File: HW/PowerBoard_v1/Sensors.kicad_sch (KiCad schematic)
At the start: 46 parts, among them U3 MCP9700AT-ETT, U4 PAMC1350DWVR, U5 PAMC1350DWVR, U6 PAMC1350DWVR, U7 PAMC1350DWVR, U8 3v3 ISO DC/DC

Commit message: updated naming
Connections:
- net SHUNT OUT is gone; now on net Batt In: R11.1, TP11.1, U7.2 (INP)
- net Batt IN+ renamed Batt In
- net Batt Out+ renamed Batt Out
- net SHUNT IN renamed Sol Out
- net Solar IN+ renamed Sol In
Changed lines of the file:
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@@
 		)
 	)
+	(wire
+		(pts
+			(xy 245.11 129.54) (xy 255.27 129.54)
+		)
+		(stroke
+			(width 0)
+			(type default)
+		)
+	)
 	(polyline
 		(pts
@@
 	(wire
 		(pts
-			(xy 259.08 134.62) (xy 245.11 134.62)
+			(xy 255.27 134.62) (xy 245.11 134.62)
 		)
 		(stroke
@@
 	(wire
 		(pts
-			(xy 245.11 139.7) (xy 259.08 139.7)
+			(xy 245.11 139.7) (xy 255.27 139.7)
 		)
 		(stroke
@@
 	(wire
 		(pts
-			(xy 259.08 129.54) (xy 245.11 129.54)
-		)
-		(stroke
-			(width 0)
-			(type default)
-		)
-	)
-	(wire
-		(pts
 			(xy 127 71.12) (xy 124.46 71.12)
 		)
@@
 	(wire
 		(pts
-			(xy 245.11 124.46) (xy 259.08 124.46)
+			(xy 245.11 124.46) (xy 255.27 124.46)
 		)
 		(stroke
@@
 		)
 	)
-	(label "I- Sense Batt"
-		(at 179.07 146.05 180)
+	(label "Sol Out"
+		(at 265.43 83.82 180)
 		(fields_autoplaced yes)
 		(effects
@@
 		)
 	)
-	(label "ADC V Batt"
-		(at 53.34 38.1 180)
+	(label "Batt In"
+		(at 179.07 143.51 180)
 		(fields_autoplaced yes)
 		(effects
@@
 		)
 	)
-	(label "I- Sense Sol"
-		(at 265.43 83.82 180)
+	(label "ADC V Batt"
+		(at 53.34 38.1 180)
 		(fields_autoplaced yes)
 		(effects
@@
 		)
 	)
+	(label "Batt In"
+		(at 261.62 31.75 0)
+		(fields_autoplaced yes)
+		(effects
+			(font
+				(size 1.27 1.27)
+			)
+			(justify left bottom)
+		)
+	)
 	(label "V Sense Sol"
 		(at 234.95 49.53 180)
@@
 		)
 	)
-	(label "I+ Sense Sol"
+	(label "Sol In"
 		(at 245.11 124.46 0)
 		(fields_autoplaced yes)
@@
 		)
 	)
-	(label "I+ Sense Sol"
-		(at 232.41 83.82 0)
+	(label "ADC V Sol"
+		(at 116.84 66.04 0)
 		(fields_autoplaced yes)
 		(effects
@@
 		)
 	)
-	(label "ADC V Sol"
-		(at 116.84 66.04 0)
+	(label "Sol In"
+		(at 179.07 121.92 180)
 		(fields_autoplaced yes)
 		(effects
@@
 				(size 1.27 1.27)
 			)
-			(justify left bottom)
+			(justify right bottom)
 		)
 	)
-	(label "I- Sense Sol"
-		(at 179.07 124.46 180)
+	(label "V Sense Batt"
+		(at 257.81 49.53 180)
 		(fields_autoplaced yes)
 		(effects
@@
 		)
 	)
-	(label "I- Sense Batt"
-		(at 265.43 93.98 180)
+	(label "Batt In"
+		(at 232.41 93.98 0)
+		(fields_autoplaced yes)
+		(effects
+			(font
+				(size 1.27 1.27)
+			)
+			(justify left bottom)
+		)
+	)
+	(label "Sol Out"
+		(at 179.07 124.46 180)
 		(fields_autoplaced yes)
 		(effects
@@
 		)
 	)
-	(label "V Sense Batt"
-		(at 257.81 49.53 180)
+	(label "Sol Out"
+		(at 252.73 129.54 180)
 		(fields_autoplaced yes)
 		(effects
@@
 		)
 	)
-	(label "Solar IN+"
-		(at 238.76 31.75 0)
+	(label "Sol In"
+		(at 232.41 83.82 0)
 		(fields_autoplaced yes)
 		(effects
@@
 		)
 	)
-	(label "I- Sense Sol"
-		(at 257.81 129.54 180)
+	(label "Batt Out"
+		(at 179.07 146.05 180)
 		(fields_autoplaced yes)
 		(effects
@@
 		)
 	)
-	(label "I+ Sense Sol"
-		(at 179.07 121.92 180)
+	(label "Batt Out"
+		(at 265.43 93.98 180)
 		(fields_autoplaced yes)
 		(effects
@@
 		)
 	)
-	(label "I- Sense Batt"
+	(label "Batt Out"
 		(at 245.11 139.7 0)
 		(fields_autoplaced yes)
@@
 		)
 	)
-	(label "I+ Sense Batt"
-		(at 179.07 143.51 180)
-		(fields_autoplaced yes)
-		(effects
-			(font
-				(size 1.27 1.27)
-			)
-			(justify right bottom)
-		)
-	)
-	(label "I+ Sense Batt"
-		(at 232.41 93.98 0)
-		(fields_autoplaced yes)
-		(effects
-			(font
-				(size 1.27 1.27)
-			)
-			(justify left bottom)
-		)
-	)
-	(label "Batt IN+"
-		(at 261.62 31.75 0)
+	(label "Sol In"
+		(at 238.76 31.75 0)
 		(fields_autoplaced yes)
 		(effects
@@
 		)
 	)
-	(label "I+ Sense Batt"
+	(label "Batt In"
 		(at 245.11 134.62 0)
 		(fields_autoplaced yes)
@@
 		)
 	)
-	(hierarchical_label "SHUNT OUT"
+	(hierarchical_label "Batt In"
 		(shape input)
-		(at 259.08 134.62 0)
+		(at 255.27 134.62 0)
 		(fields_autoplaced yes)
 		(effects
@@
 		)
 	)
-	(hierarchical_label "Solar IN+"
+	(hierarchical_label "Sol In"
 		(shape input)
-		(at 259.08 124.46 0)
+		(at 255.27 124.46 0)
 		(fields_autoplaced yes)
 		(effects
@@
 		)
 	)
-	(hierarchical_label "Batt Out+"
+	(hierarchical_label "Batt Out"
 		(shape output)
-		(at 259.08 139.7 0)
+		(at 255.27 139.7 0)
 		(fields_autoplaced yes)
 		(effects
@@
 		)
 	)
-	(hierarchical_label "SHUNT IN"
+	(hierarchical_label "Sol Out"
 		(shape output)
-		(at 259.08 129.54 0)
+		(at 255.27 129.54 0)
 		(fields_autoplaced yes)
 		(effects
@@
 					(size 1.27 1.27)
 				)
+				(hide yes)
 			)
 		)

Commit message: name changes
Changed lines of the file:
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@@
 	)
 	(junction
+		(at 133.35 25.4)
+		(diameter 0)
+		(color 0 0 0 0)
+	)
+	(junction
 		(at 161.29 43.18)
 		(diameter 0)
@@
 	(wire
 		(pts
+			(xy 133.35 24.13) (xy 133.35 25.4)
+		)
+		(stroke
+			(width 0)
+			(type default)
+		)
+	)
+	(wire
+		(pts
 			(xy 165.1 31.75) (xy 165.1 33.02)
 		)
@@
 	(text "+3.3VA represents the High Voltage 3.3v side. "
 		(exclude_from_sim no)
-		(at 155.956 22.098 0)
+		(at 171.196 21.844 0)
 		(effects
 			(font
@@
 					(unit 1)
 				)
+			)
+		)
+	)
+	(symbol
+		(lib_id "power:PWR_FLAG")
+		(at 133.35 24.13 0)
+		(unit 1)
+		(exclude_from_sim no)
+		(in_bom yes)
+		(on_board yes)
+		(dnp no)
+		(property "Reference" "#FLG03"
+			(at 133.35 22.225 0)
+			(effects
+				(font
+					(size 1.27 1.27)
+				)
+				(hide yes)
+			)
+		)
+		(property "Value" "PWR_FLAG"
+			(at 133.35 20.066 0)
+			(effects
+				(font
+					(size 1.27 1.27)
+				)
+			)
+		)
+		(property "Footprint" ""
+			(at 133.35 24.13 0)
+			(effects
+				(font
+					(size 1.27 1.27)
+				)
+				(hide yes)
+			)
+		)
+		(property "Datasheet" "~"
+			(at 133.35 24.13 0)
+			(effects
+				(font
+					(size 1.27 1.27)
+				)
+				(hide yes)
+			)
+		)
+		(property "Description" "Special symbol for telling ERC where power comes from"
+			(at 133.35 24.13 0)
+			(effects
+				(font
+					(size 1.27 1.27)
+				)
+				(hide yes)
+			)
+		)
+		(pin "1"
+		)
+		(instances
+			(project "power_v1"
+				(path "/1e1b062d-fad0-427c-a622-c5b8a80b5268/f37b00a5-62bb-47d6-b18e-0a47b6349fc3"
+					(reference "#FLG03")
+					(unit 1)
+				)

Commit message: small layout changes
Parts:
- U4, U5, U6, U7: footprint U_PAMC1350DWVR_TEX -> layout:U_PAMC1350DWVR_TEX
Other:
- company: (none) -> Illini Solar Car
- title: (none) -> Power Board v1
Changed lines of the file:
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@@
 	(paper "A4")
 	(title_block
+		(title "Power Board v1")
+		(date "2024-03-04")
+		(rev "1")
+		(company "Illini Solar Car")
 		(comment 1 "Designed By: Alex Lymberopoulos & Alex Chmiel & Akhil Pothineni")
 	)
@@
 			)
 		)
-		(property "Footprint" "U_PAMC1350DWVR_TEX"
+		(property "Footprint" "layout:U_PAMC1350DWVR_TEX"
 			(at 167.64 119.38 0)
 			(effects
@@
 			)
 		)
-		(property "Footprint" "U_PAMC1350DWVR_TEX"
+		(property "Footprint" "layout:U_PAMC1350DWVR_TEX"
 			(at 167.64 140.97 0)
 			(effects
@@
 			)
 		)
-		(property "Footprint" "U_PAMC1350DWVR_TEX"
+		(property "Footprint" "layout:U_PAMC1350DWVR_TEX"
 			(at 167.64 63.5 0)
 			(effects
@@
 			)
 		)
-		(property "Footprint" "U_PAMC1350DWVR_TEX"
+		(property "Footprint" "layout:U_PAMC1350DWVR_TEX"
 			(at 167.64 85.09 0)
 			(effects

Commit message: more layout
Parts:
- R10, R11: footprint Package_TO_SOT_SMD:TO-263-2_TabPin1 -> Package_TO_SOT_SMD:TO-263-2_isolatedback
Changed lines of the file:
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@@
 			)
 		)
-		(property "Footprint" "Package_TO_SOT_SMD:TO-263-2_TabPin1"
+		(property "Footprint" "Package_TO_SOT_SMD:TO-263-2_isolatedback"
 			(at 249.174 92.964 90)
 			(effects
@@
 			)
 		)
-		(property "Footprint" "Package_TO_SOT_SMD:TO-263-2_TabPin1"
+		(property "Footprint" "Package_TO_SOT_SMD:TO-263-2_isolatedback"
 			(at 249.174 82.804 90)
 			(effects

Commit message: pushed board
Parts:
- removed TP10: ADC V Sol, TestPoint:TestPoint_THTPad_1.0x1.0mm_Drill0.5mm, symbol Connector:TestPoint
- removed TP12: ADC I Sol, TestPoint:TestPoint_THTPad_1.0x1.0mm_Drill0.5mm, symbol Connector:TestPoint
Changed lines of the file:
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@@
 		)
 	)
-	(wire
-		(pts
-			(xy 245.11 129.54) (xy 255.27 129.54)
-		)
-		(stroke
-			(width 0)
-			(type default)
-		)
-	)
 	(polyline
 		(pts
@@
 	(wire
 		(pts
+			(xy 245.11 129.54) (xy 255.27 129.54)
+		)
+		(stroke
+			(width 0)
+			(type default)
+		)
+	)
+	(wire
+		(pts
 			(xy 127 87.63) (xy 116.84 87.63)
 		)
@@
 	)
 	(label "Sol Out"
-		(at 252.73 129.54 180)
+		(at 245.11 129.54 0)
 		(fields_autoplaced yes)
 		(effects
@@
 				(size 1.27 1.27)
 			)
-			(justify right bottom)
+			(justify left bottom)
 		)
 	)
@@
 	)
 	(symbol
-		(lib_id "Connector:TestPoint")
-		(at 245.11 139.7 90)
-		(unit 1)
-		(exclude_from_sim no)
-		(in_bom yes)
-		(on_board yes)
-		(dnp no)
-		(property "Reference" "TP10"
-			(at 239.776 141.478 90)
-			(effects
-				(font
-					(size 1.27 1.27)
-				)
-				(justify left)
-			)
-		)
-		(property "Value" "ADC V Sol"
-			(at 240.284 139.7 90)
-			(effects
-				(font
-					(size 1.27 1.27)
-				)
-				(justify left)
-			)
-		)
-		(property "Footprint" "TestPoint:TestPoint_THTPad_1.0x1.0mm_Drill0.5mm"
-			(at 245.11 134.62 0)
-			(effects
-				(font
-					(size 1.27 1.27)
-				)
-				(hide yes)
-			)
-		)
-		(property "Datasheet" "~"
-			(at 245.11 134.62 0)
-			(effects
-				(font
-					(size 1.27 1.27)
-				)
-				(hide yes)
-			)
-		)
-		(property "Description" "test point"
-			(at 245.11 139.7 0)
-			(effects
-				(font
-					(size 1.27 1.27)
-				)
-				(hide yes)
-			)
-		)
-		(pin "1"
-		)
-		(instances
-			(project "power_v1"
-				(path "/1e1b062d-fad0-427c-a622-c5b8a80b5268/f37b00a5-62bb-47d6-b18e-0a47b6349fc3"
-					(reference "TP10")
-					(unit 1)
-				)
-			)
-		)
-	)
-	(symbol
 		(lib_id "device:C")
 		(at 189.23 67.31 0)
@@
 					(unit 1)
 				)
-			)
-		)
-	)
-	(symbol
-		(lib_id "Connector:TestPoint")
-		(at 245.11 129.54 90)
-		(unit 1)
-		(exclude_from_sim no)
-		(in_bom yes)
-		(on_board yes)
-		(dnp no)
-		(property "Reference" "TP12"
-			(at 239.776 131.318 90)
-			(effects
-				(font
-					(size 1.27 1.27)
-				)
-				(justify left)
-			)
-		)
-		(property "Value" "ADC I Sol"
-			(at 240.284 129.54 90)
-			(effects
-				(font
-					(size 1.27 1.27)
-				)
-				(justify left)
-			)
-		)
-		(property "Footprint" "TestPoint:TestPoint_THTPad_1.0x1.0mm_Drill0.5mm"
-			(at 245.11 124.46 0)
-			(effects
-				(font
-					(size 1.27 1.27)
-				)
-				(hide yes)
-			)
-		)
-		(property "Datasheet" "~"
-			(at 245.11 124.46 0)
-			(effects
-				(font
-					(size 1.27 1.27)
-				)
-				(hide yes)
-			)
-		)
-		(property "Description" "test point"
-			(at 245.11 129.54 0)
-			(effects
-				(font
-					(size 1.27 1.27)
-				)
-				(hide yes)
-			)
-		)
-		(pin "1"
-		)
-		(instances
-			(project "power_v1"
-				(path "/1e1b062d-fad0-427c-a622-c5b8a80b5268/f37b00a5-62bb-47d6-b18e-0a47b6349fc3"
-					(reference "TP12")
-					(unit 1)
-				)

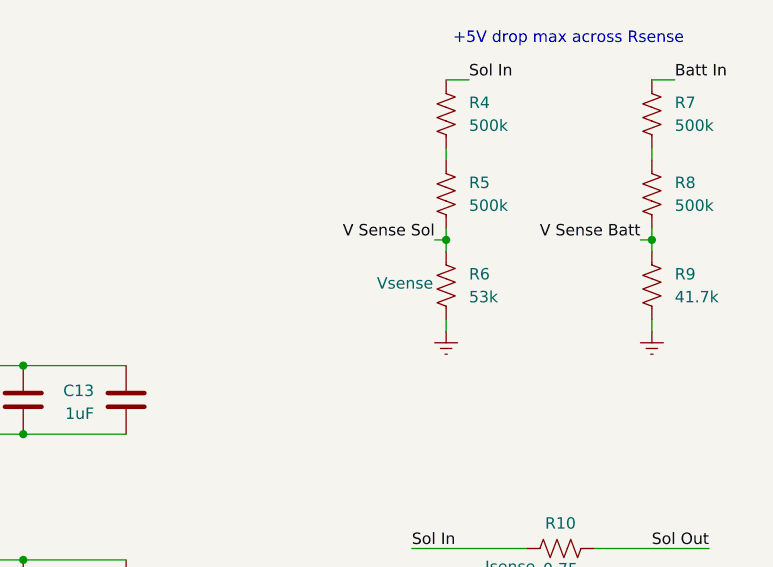
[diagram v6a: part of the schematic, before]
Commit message: added ti paper for resistor sizing
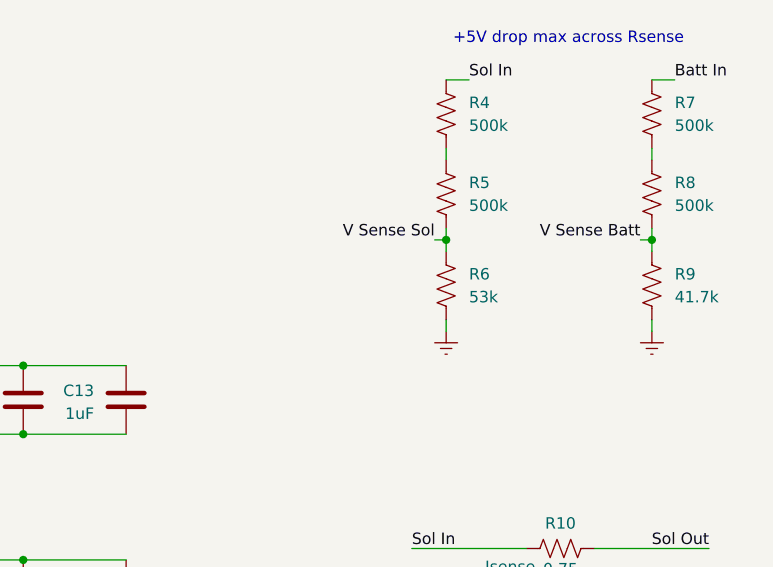
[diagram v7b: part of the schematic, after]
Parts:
- R6, R9: Note Vsense -> https://www.ti.com/lit/an/sbaa350a/sbaa350a.pdf?ts=17110032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
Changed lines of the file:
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@@
 			)
 		)
-		(property "Note" "Vsense"
+		(property "Note" "https://www.ti.com/lit/an/sbaa350a/sbaa350a.pdf?ts=1711003254897&ref_url=https%253A%252F%252Fwww.ti.com%252Fproduct%252Fde-de%252FAMC1300B-Q1"
 			(at 231.648 54.356 0)
 			(effects
@@
 					(size 1.27 1.27)
 				)
+				(hide yes)
 			)
 		)
@@
 			)
 		)
-		(property "Note" "Vsense"
+		(property "Note" "https://www.ti.com/lit/an/sbaa350a/sbaa350a.pdf?ts=1711003254897&ref_url=https%253A%252F%252Fwww.ti.com%252Fproduct%252Fde-de%252FAMC1300B-Q1"
 			(at 254.508 54.356 0)
 			(effects

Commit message: pushed changes
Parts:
- R10, R11: Note Isense -> https://www.ti.com/lit/an/slyt810/slyt810.pdf?ts=1711017523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
- R4, R5, R7, R8: MPN (none) -> 499K Ohm 1% 1/10W
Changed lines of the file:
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@@
 			)
 		)
-		(property "Note" "Isense"
+		(property "Note" "https://www.ti.com/lit/an/slyt810/slyt810.pdf?ts=1711017523209&ref_url=https%253A%252F%252Fwww.ti.com%252Ftechnologies%252Fcurrent-sensing-solutions.html"
 			(at 243.332 96.012 90)
 			(effects
@@
 					(size 1.27 1.27)
 				)
+				(hide yes)
 			)
 		)
@@
 			)
 		)
+		(property "MPN" "499K Ohm 1% 1/10W"
+			(at 259.08 44.45 0)
+			(effects
+				(font
+					(size 1.27 1.27)
+				)
+				(hide yes)
+			)
+		)
 		(pin "2"
 		)
@@
 			)
 		)
+		(property "MPN" "499K Ohm 1% 1/10W"
+			(at 236.22 44.45 0)
+			(effects
+				(font
+					(size 1.27 1.27)
+				)
+				(hide yes)
+			)
+		)
 		(pin "2"
 		)
@@
 			)
 		)
-		(property "Note" "Isense"
+		(property "Note" "https://www.ti.com/lit/an/slyt810/slyt810.pdf?ts=1711017523209&ref_url=https%253A%252F%252Fwww.ti.com%252Ftechnologies%252Fcurrent-sensing-solutions.html"
 			(at 243.332 85.852 90)
 			(effects
@@
 					(size 1.27 1.27)
 				)
+				(hide yes)
 			)
 		)
@@
 			)
 		)
+		(property "MPN" "499K Ohm 1% 1/10W"
+			(at 236.22 35.56 0)
+			(effects
+				(font
+					(size 1.27 1.27)
+				)
+				(hide yes)
+			)
+		)
 		(pin "2"
 		)
@@
 			(at 259.08 35.56 0)
 			(effects
+				(font
+					(size 1.27 1.27)
+				)
+				(hide yes)
+			)
+		)
+		(property "MPN" "499K Ohm 1% 1/10W"
+			(at 259.08 35.56 0)
+			(effects
